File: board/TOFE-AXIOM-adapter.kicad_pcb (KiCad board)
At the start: 4 copper layers, 68.9 x 31.9 mm, 21 parts, among them CN1 C, U1 24AA01/24LC01B, U2 LM317T, U3 LM7805CT

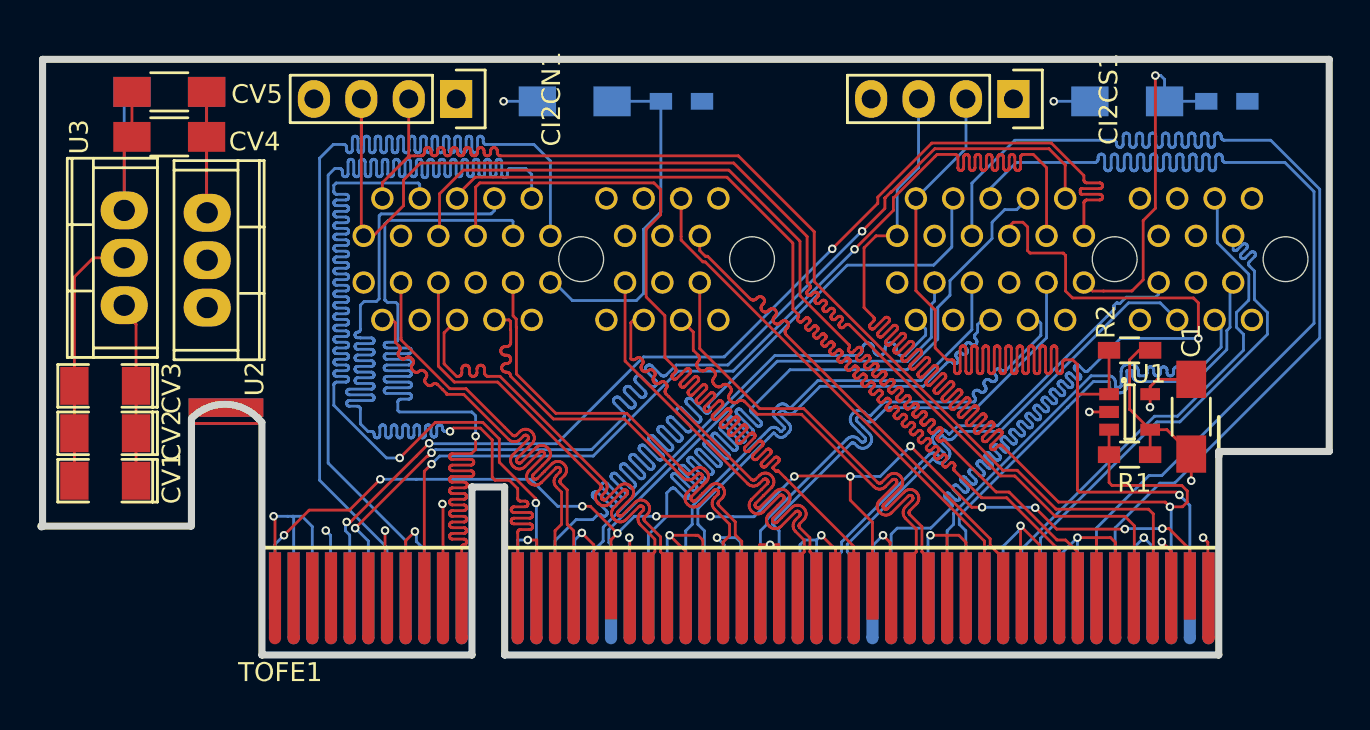
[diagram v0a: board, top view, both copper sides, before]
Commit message: Fixing DRC caused by wrong via size usage.
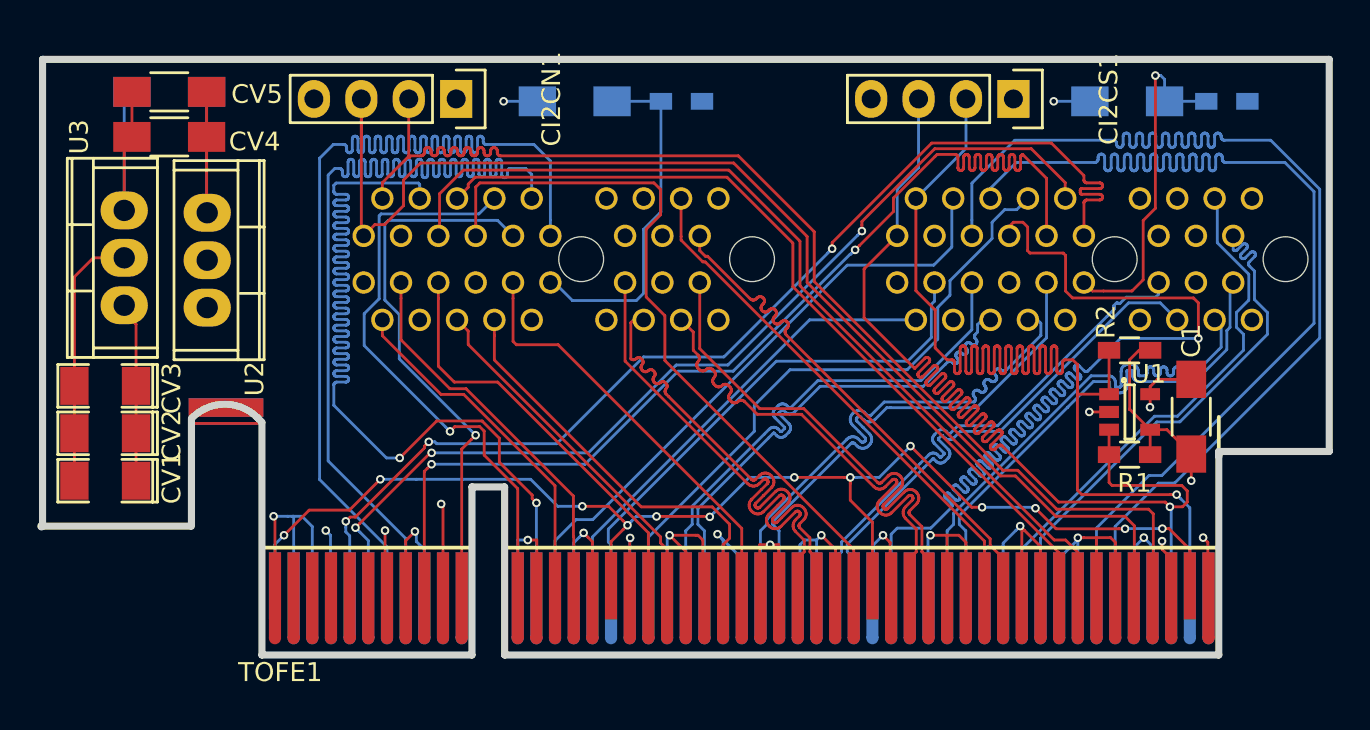
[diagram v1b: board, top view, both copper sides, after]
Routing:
- net /N_IO5: track 60.1 -> 29.5 mm
- net /N_IO4: track 60.1 -> 31.9 mm
- net /S_IO0: track 60.0 -> 33.3 mm
- net /S_IO4: track 60.1 -> 33.7 mm
- net /N_IO3: track 60.1 -> 39.4 mm
- net /N_IO2: track 60.2 -> 44.8 mm
- net /N_IO1: track 60.1 -> 49.2 mm
- net /S_SDA: track 76.9 -> 66.4 mm
- net /N_LVDS_0_P: track 28.1 -> 19.3 mm
- net /N_LVDS_1_N: track 28.1 -> 19.4 mm
- net /S_IO6: track 60.1 -> 52.2 mm
- net /N_LVDS_0_N: track 28.1 -> 21.1 mm
- net /N_LVDS_2_P: track 28.1 -> 22.3 mm
- net /N_LVDS_1_P: track 28.1 -> 22.8 mm
- net /N_LVDS_2_N: track 28.1 -> 23.1 mm
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
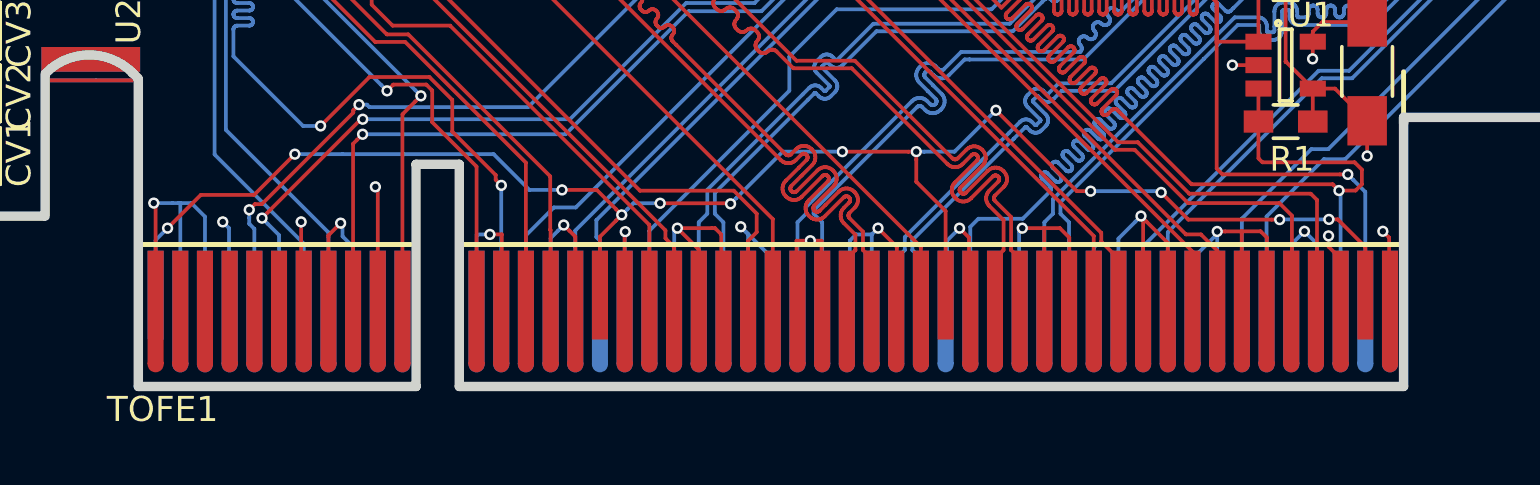
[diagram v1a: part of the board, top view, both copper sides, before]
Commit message: Fixing more DRC errors.
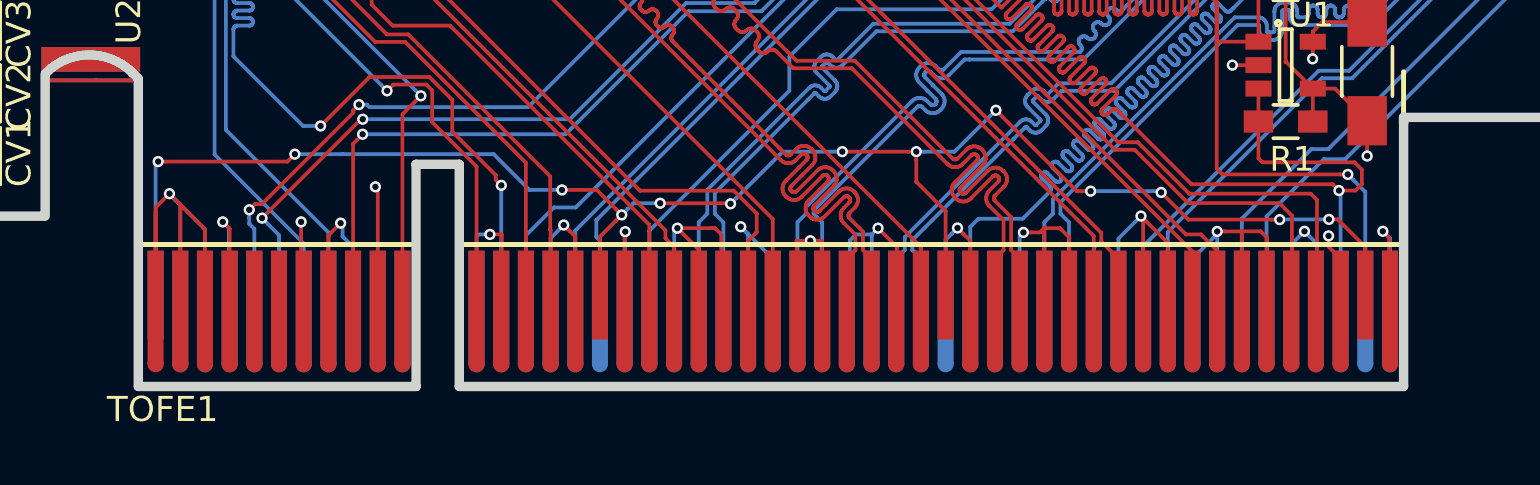
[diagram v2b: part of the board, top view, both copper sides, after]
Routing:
- net GND: track 165.5 -> 257.3 mm
- net /VCC12V: track 46.1 -> 71.2 mm
- net /VCC3V3: track 66.7 -> 75.9 mm
- net /S_LVDS_5_N: track 28.1 -> 30.4 mm
- net /S_LVDS_5_P: track 28.1 -> 30.4 mm
- net /S_LVDS_4_P: track 28.0 -> 30.3 mm
- net /N_LVDS_5_N: track 28.1 -> 30.4 mm
- net /S_LVDS_2_P: track 28.1 -> 30.4 mm
- net /N_LVDS_0_N: track 21.1 -> 23.4 mm
- net Net-(TOFE1-PadA33): track 0.00 -> 2.30 mm
- net /S_SDA: track 66.4 -> 68.7 mm
- net /S_SCL: track 72.3 -> 74.6 mm
- net /S_LVDS_4_N: track 28.0 -> 30.3 mm
- net /S_LVDS_3_P: track 28.0 -> 30.3 mm
- net /S_LVDS_2_N: track 28.1 -> 30.4 mm
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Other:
- net class PWR added: clearance 0.1524, trace_width 0.4572, via_dia 0.4572, via_drill 0.254

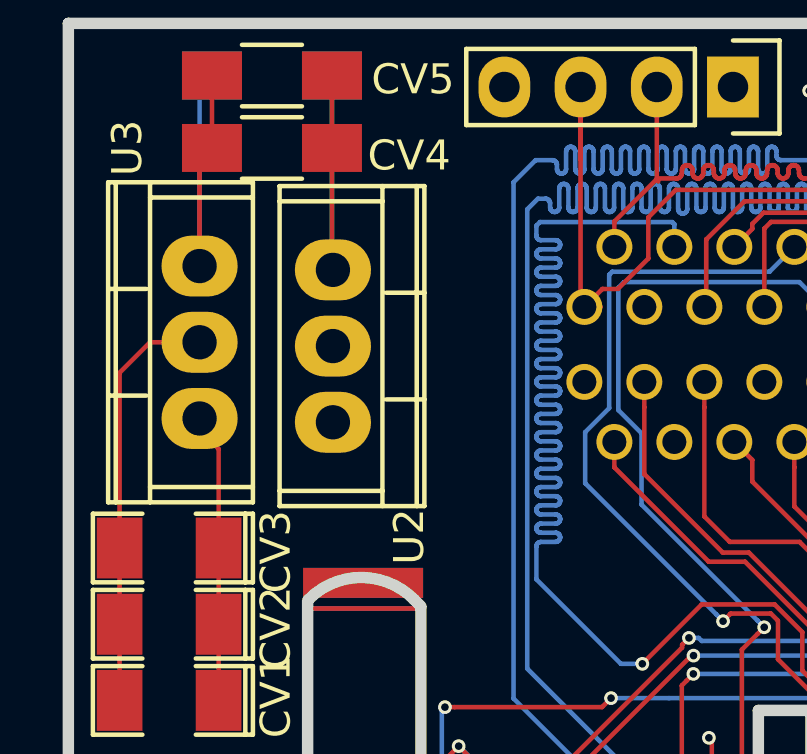
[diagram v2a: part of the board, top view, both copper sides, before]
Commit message: Using the inner layer for VCC routing.
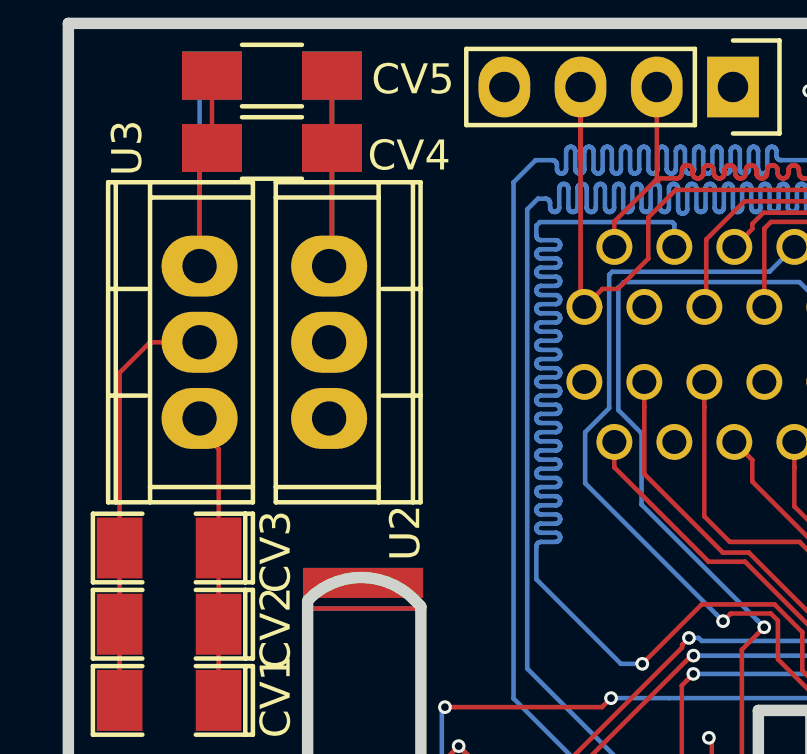
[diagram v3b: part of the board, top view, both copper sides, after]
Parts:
- moved U2 0.18 mm to (170.9, 166.9)
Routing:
- added copper zone on In2.Cu, net /VCC12V
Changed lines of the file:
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@@
     (thickness 1.6)
     (drawings 25)
-    (tracks 5763)
+    (tracks 5764)
     (zones 0)
     (modules 21)
@@
   )
   (layers
-    (0 F.Cu signal)
+    (0 F.Cu signal hide)
     (1 In1.Cu signal hide)
     (2 In2.Cu signal hide)
-    (31 B.Cu signal)
+    (31 B.Cu signal hide)
     (32 B.Adhes user)
     (33 F.Adhes user)
     (34 B.Paste user)
     (35 F.Paste user)
-    (36 B.SilkS user)
+    (36 B.SilkS user hide)
     (37 F.SilkS user)
     (38 B.Mask user)
-    (39 F.Mask user)
+    (39 F.Mask user hide)
     (40 Dwgs.User user hide)
     (41 Cmts.User user)
@@
   )
   (module Power_Integrations:TO-220 (layer F.Cu)
-    (at 171.069 167.005 270)
+    (at 170.942 166.878 270)
     (descr "Non Isolated JEDEC TO-220 Package")
     (tags "Power Integration YN Package")
@@
   (segment (start 218.02492 168.19968) (end 218.02492 168.43608) (width 0.1524) (layer F.Cu) (net 58))
   (segment (start 224.579 158.496) (end 222.345 158.496) (width 0.1524) (layer B.Cu) (net 58))
+  (segment (start 171.069 167.005) (end 170.815 167.005) (width 0.1524) (layer In2.Cu) (net 61))
+  (segment (start 170.815 167.005) (end 168.148 164.338) (width 0.1524) (layer In2.Cu) (net 61))
+  (segment (start 168.148 164.338) (end 166.624 164.338) (width 0.1524) (layer In2.Cu) (net 61))
   (segment (start 166.624 164.338) (end 166.624 158.401) (width 0.1524) (layer B.Cu) (net 61))
   (segment (start 166.624 158.401) (end 167.037 157.988) (width 0.1524) (layer B.Cu) (net 61))
-  (segment (start 171.069 167.005) (end 169.291 167.005) (width 0.1524) (layer In2.Cu) (net 61))
-  (segment (start 169.291 167.005) (end 166.624 164.338) (width 0.1524) (layer In2.Cu) (net 61))
   (segment (start 167.037 157.988) (end 167.037 160.401) (width 0.1524) (layer F.Cu) (net 61))
   (segment (start 167.037 160.401) (end 166.624 160.814) (width 0.1524) (layer F.Cu) (net 61))
@@
       )
     )
+  )
+  (zone (net 3) (net_name /VCC12V) (layer In2.Cu) (hatch edge 0.508)
+    (connect_pads (clearance 0.1524))
+    (min_thickness 0.254)
+    (fill yes (arc_segments 16) (thermal_gap 0.508) (thermal_bridge_width 0.508))
+    (polygon
+      (pts
+        (xy 174.244 187.706) (xy 177.038 187.706) (xy 177.038 173.736) (xy 172.212 168.402) (xy 162.306 168.402)
+        (xy 162.306 181.356) (xy 170.18 181.356) (xy 170.18 174.244) (xy 174.244 174.244)
+      )
+    )

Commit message: Updating netlist and adding VCC polygons.
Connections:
- net /VCC_5V0 renamed /VCC5V0
- CI2CN1 pad 1: /VCC_3V3 -> /VCC3V3
- CI2CS1 pad 1: /VCC_3V3 -> /VCC3V3
- NORTH1 pad B13: /VCC_3V3 -> /VCC3V3
- NORTH1 pad B3: /VCC_3V3 -> /VCC3V3
- SOUTH1 pad B13: /VCC_3V3 -> /VCC3V3
- SOUTH1 pad B3: /VCC_3V3 -> /VCC3V3
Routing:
- net /VCC_3V3: track 66.5 -> 0.00 mm
- net /VCC3V3: track 75.9 -> 142.4 mm
- added copper zone on In2.Cu, net /VCC5V0
- added copper zone on In2.Cu, net /VCC_3V3

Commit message: More power supply planes.
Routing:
- net /VCC3V3: track 142.4 -> 95.1 mm
- net /VCC5V0: track 32.1 -> 0.00 mm
- net /VCC5V: track 18.6 -> 13.0 mm
- added copper zone on In2.Cu, net /VCC3V3
- removed copper zone on In2.Cu, net /VCC_3V3

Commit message: More power fixes.
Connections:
- CV4 pad 1: /VCC5V -> /VCC5V0
- CV5 pad 1: /VCC5V -> /VCC5V0
- CV6 pad 1: /VCC5V -> /VCC5V0
- U2 pad 2: /VCC5V -> /VCC5V0
- U3 pad 3: /VCC5V -> /VCC5V0
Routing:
- net /VCC5V0: track 0.00 -> 13.0 mm
- net /VCC5V: track 13.0 -> 0.00 mm
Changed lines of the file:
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@@
 (kicad_pcb (version 4) (host pcbnew 4.0.2-4+6225~38~ubuntu14.04.1-stable)
   (general
-    (links 249)
-    (no_connects 2)
-    (area 161.000001 151.4 231.378602 190.0677)
+    (links 250)
+    (no_connects 5)
+    (area 162.059499 156.057599 231.355901 188.340501)
     (thickness 1.6)
     (drawings 25)
@@
     (zones 0)
     (modules 21)
-    (nets 61)
+    (nets 60)
   )
   (page A3)
@@
   (net 57 "Net-(RS1-Pad1)")
   (net 58 "Net-(SOUTH1-PadB14)")
-  (net 59 /VCC5V)
-  (net 60 /VCC5V0)
+  (net 59 /VCC5V0)
   (net_class Default "This is the default net class."
     (clearance 0.1524)
@@
     (add_net /VCC12V)
     (add_net /VCC3V3)
-    (add_net /VCC5V)
     (add_net GND)
   )
@@
       (net 55 /S_LVDS_5_N))
     (pad B12 thru_hole circle (at 3.50012 -3.2512) (size 1.19888 1.19888) (drill 0.8001) (layers *.Cu *.Mask)
-      (net 60 /VCC5V0))
+      (net 59 /VCC5V0))
     (pad B14 thru_hole circle (at 5.4991 -3.2512) (size 1.19888 1.19888) (drill 0.8001) (layers *.Cu *.Mask)
       (net 58 "Net-(SOUTH1-PadB14)"))
@@
       (net 36 /N_LVDS_5_N))
     (pad B12 thru_hole circle (at 3.50012 -3.2512) (size 1.19888 1.19888) (drill 0.8001) (layers *.Cu *.Mask)
-      (net 60 /VCC5V0))
+      (net 59 /VCC5V0))
     (pad B14 thru_hole circle (at 5.4991 -3.2512) (size 1.19888 1.19888) (drill 0.8001) (layers *.Cu *.Mask)
       (net 27 "Net-(NORTH1-PadB14)"))
@@
     (fp_line (start -1 1.025) (end 1 1.025) (layer F.SilkS) (width 0.15))
     (pad 1 smd rect (at -2 0) (size 2 1.6) (layers F.Cu F.Paste F.Mask)
-      (net 59 /VCC5V))
+      (net 59 /VCC5V0))
     (pad 2 smd rect (at 2 0) (size 2 1.6) (layers F.Cu F.Paste F.Mask)
       (net 5 GND))
@@
     (fp_line (start -1 1.025) (end 1 1.025) (layer F.SilkS) (width 0.15))
     (pad 1 smd rect (at -2 0) (size 2 1.6) (layers F.Cu F.Paste F.Mask)
-      (net 59 /VCC5V))
+      (net 59 /VCC5V0))
     (pad 2 smd rect (at 2 0) (size 2 1.6) (layers F.Cu F.Paste F.Mask)
       (net 5 GND))
@@
     (fp_line (start -1 -1.025) (end 1 -1.025) (layer B.SilkS) (width 0.15))
     (pad 1 smd rect (at -2 0) (size 2 1.6) (layers B.Cu B.Paste B.Mask)
-      (net 59 /VCC5V))
+      (net 59 /VCC5V0))
     (pad 2 smd rect (at 2 0) (size 2 1.6) (layers B.Cu B.Paste B.Mask)
       (net 5 GND))
@@
     (fp_line (start 5.334 -3.048) (end -5.334 -3.048) (layer F.SilkS) (width 0.15))
     (pad 2 thru_hole oval (at 0 0 270) (size 2.032 2.54) (drill 1.143) (layers *.Cu *.Mask F.SilkS)
-      (net 59 /VCC5V))
+      (net 59 /VCC5V0))
     (pad 3 thru_hole oval (at 2.54 0 270) (size 2.032 2.54) (drill 1.143) (layers *.Cu *.Mask F.SilkS)
       (net 3 /VCC12V))
@@
       (net 5 GND))
     (pad 3 thru_hole oval (at 2.54 0 90) (size 2.032 2.54) (drill 1.143) (layers *.Cu *.Mask F.SilkS)
-      (net 59 /VCC5V))
+      (net 59 /VCC5V0))
     (pad 1 thru_hole oval (at -2.54 0 90) (size 2.032 2.54) (drill 1.143) (layers *.Cu *.Mask F.SilkS)
       (net 3 /VCC12V))
@@
     )
   )
-  (zone (net 60) (net_name /VCC5V0) (layer In2.Cu) (hatch edge 0.508)
+  (zone (net 59) (net_name /VCC5V0) (layer In2.Cu) (hatch edge 0.508)
     (priority 2)
-    (connect_pads (clearance 0.1524))
+    (connect_pads (clearance 0.254))
     (min_thickness 0.254)
     (fill yes (arc_segments 16) (thermal_gap 0.508) (thermal_bridge_width 0.508))
@@
   (zone (net 4) (net_name /VCC3V3) (layer In2.Cu) (hatch edge 0.508)
     (priority 1)
-    (connect_pads (clearance 0.1524))
+    (connect_pads (clearance 0.254))
     (min_thickness 0.254)
     (fill yes (arc_segments 16) (thermal_gap 0.508) (thermal_bridge_width 0.508))
